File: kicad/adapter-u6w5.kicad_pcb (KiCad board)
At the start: 2 copper layers, 107.9 x 86 mm, 4 parts, among them J1 THUMB_RIGHT_SPC_KB600, J5 THUMB LEFT BAK, J6 THUMB RIGHT SPC, J8 THUMB_LEFT_BAK_KB600

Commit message: adjust board size
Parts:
- moved J1 2.54 mm to (141.6, 134.6)
- moved J5 2.54 mm to (121.4, 129.8)
- moved J6 2.54 mm to (132.1, 129.8)
- moved J8 2.54 mm to (112.4, 134.6)
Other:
- board size 107.9 x 86 mm -> 62.9 x 11.2 mm
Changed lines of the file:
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@@
     (add_net /ROW_8)
     (add_net /ROW_9)
-    (add_net GND)
     (add_net "Net-(J1-Pad1)")
     (add_net "Net-(J1-Pad10)")
@@
   )
   (module kinx:39-53-2135 (layer F.Cu)
-    (at 112.395 137.16 180)
+    (at 112.395 134.62 180)
     (descr "\"1.25 FPC CONN ASSY ZF 13\"")
     (fp_text reference J8 (at -12.827 -0.254 180) (layer F.SilkS) hide
@@
   )
   (module Connector_PinHeader_2.54mm:PinHeader_1x10_P2.54mm_Vertical (layer B.Cu)
-    (at 121.412 132.334 90)
+    (at 121.412 129.794 90)
     (descr "Through hole straight pin header, 1x10, 2.54mm pitch, single row")
     (tags "Through hole pin header THT 1x10 2.54mm single row")
@@
   )
   (module Connector_PinHeader_2.54mm:PinHeader_1x10_P2.54mm_Vertical (layer B.Cu)
-    (at 132.08 132.334 270)
+    (at 132.08 129.794 270)
     (descr "Through hole straight pin header, 1x10, 2.54mm pitch, single row")
     (tags "Through hole pin header THT 1x10 2.54mm single row")
@@
   )
   (module kinx:39-53-2135 (layer F.Cu)
-    (at 141.605 137.16 180)
+    (at 141.605 134.62 180)
     (descr "\"1.25 FPC CONN ASSY ZF 13\"")
     (fp_text reference J1 (at 11.557 -0.254 180) (layer F.SilkS) hide
@@
       (solder_mask_margin 0.0635))
   )
-  (gr_line (start 95.25 148.0036) (end 203.2 148.0036) (layer Edge.Cuts) (width 0.05))
-  (gr_line (start 203.2 148.0036) (end 203.2 62.0036) (layer Edge.Cuts) (width 0.05))
-  (gr_line (start 203.2 62.0036) (end 95.25 62.0036) (layer Edge.Cuts) (width 0.05))
-  (gr_line (start 95.25 62.0036) (end 95.25 148.0036) (layer Edge.Cuts) (width 0.05))
-  (segment (start 148.971 136.819) (end 148.931 136.779) (width 0.25) (layer F.Cu) (net 0))
+  (gr_line (start 95.25 138.176) (end 158.115 138.176) (layer Edge.Cuts) (width 0.05))
+  (gr_line (start 158.115 138.176) (end 158.115 127) (layer Edge.Cuts) (width 0.05))
+  (gr_line (start 158.115 127) (end 95.25 127) (layer Edge.Cuts) (width 0.05))
+  (gr_line (start 95.25 127) (end 95.25 138.176) (layer Edge.Cuts) (width 0.05))
+  (segment (start 148.971 134.279) (end 148.931 134.239) (width 0.25) (layer F.Cu) (net 0))
   (zone (net 9) (net_name GND) (layer F.Cu) (hatch edge 0.508)
     (priority 6)
@@
     (polygon
       (pts
-        (xy 203.1163 147.2068) (xy 95.25 147.2068) (xy 95.25 62.8004) (xy 203.1163 62.8004)
+        (xy 157.988 138.049) (xy 95.377 138.049) (xy 95.377 127.127) (xy 157.988 127.127)
       )
     )
@@
     (polygon
       (pts
-        (xy 203.1163 147.2068) (xy 95.25 147.2068) (xy 95.25 62.8004) (xy 203.1163 62.8004)
+        (xy 157.988 138.049) (xy 95.377 138.049) (xy 95.377 127.127) (xy 157.988 127.127)
       )
     )

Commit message: panelization: add mouse bites/tab and cut lines
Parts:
- added REF**: tab, panelizationtab:tab, F.Cu at (125.9, 132.7)
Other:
- board size 62.9 x 11.2 mm -> 62.9 x 11.3 mm
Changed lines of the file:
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@@
   (general
     (thickness 1.6)
-    (drawings 4)
+    (drawings 6)
     (tracks 1)
     (zones 0)
-    (modules 4)
+    (modules 5)
     (nets 12)
   )
@@
   (setup
     (last_trace_width 0.25)
+    (user_trace_width 2.54)
     (trace_clearance 0.1524)
     (zone_clearance 0.2)
@@
     (add_net "Net-(J1-Pad2)")
     (add_net "Net-(J1-Pad9)")
-    (add_net "Net-(J5-Pad10)")
-    (add_net "Net-(J5-Pad6)")
-    (add_net "Net-(J5-Pad7)")
-    (add_net "Net-(J5-Pad9)")
     (add_net "Net-(J6-Pad1)")
     (add_net "Net-(J6-Pad10)")
@@
     (add_net "Net-(J8-Pad7)")
     (add_net "Net-(J8-Pad8)")
+  )
+  (module panelizationtab:tab (layer F.Cu)
+    (at 125.857 132.715 90)
+    (fp_text reference REF** (at 0 0.5 90) (layer F.SilkS) hide
+      (effects (font (size 1 1) (thickness 0.15)))
+    )
+    (fp_text value tab (at 0 -0.5 90) (layer F.Fab) hide
+      (effects (font (size 1 1) (thickness 0.15)))
+    )
+    (pad 4 thru_hole circle (at -1.016 1.905 90) (size 0.51 0.51) (drill 0.254) (layers *.Cu *.Mask))
+    (pad 6 thru_hole circle (at 1.016 1.905 90) (size 0.51 0.51) (drill 0.254) (layers *.Cu *.Mask))
+    (pad 5 thru_hole circle (at 0 1.905 90) (size 0.51 0.51) (drill 0.254) (layers *.Cu *.Mask))
+    (pad 1 thru_hole circle (at -1.016 0 90) (size 0.51 0.51) (drill 0.254) (layers *.Cu *.Mask))
+    (pad 3 thru_hole circle (at 1.016 0 90) (size 0.51 0.51) (drill 0.254) (layers *.Cu *.Mask))
+    (pad 2 thru_hole circle (at 0 0 90) (size 0.51 0.51) (drill 0.254) (layers *.Cu *.Mask))
   )
   (module kinx:39-53-2135 (layer F.Cu)
@@
       (solder_mask_margin 0.0635))
   )
+  (gr_line (start 126.746 135.128) (end 126.746 138.303) (layer Edge.Cuts) (width 2.54))
+  (gr_line (start 126.746 127) (end 126.746 130.302) (layer Edge.Cuts) (width 2.54))
   (gr_line (start 95.25 138.176) (end 158.115 138.176) (layer Edge.Cuts) (width 0.05))
   (gr_line (start 158.115 138.176) (end 158.115 127) (layer Edge.Cuts) (width 0.05))

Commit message: route
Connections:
- net /ROW_2 renamed /ROW_2_L
- net /ROW_3 renamed /ROW_3_L
- net /ROW_4 renamed /ROW_4_L
- net /ROW_5 renamed /ROW_5_L
- net /ROW_6 renamed /ROW_6_R
- net /ROW_7 renamed /ROW_7_R
- net /ROW_8 renamed /ROW_8_R
- net /ROW_9 renamed /ROW_9_R
- J1 pad 1: (no net) -> Net-(J1-Pad1)
- J1 pad 10: (no net) -> Net-(J1-Pad10)
- J1 pad 11: (no net) -> Net-(J1-Pad11)
- J1 pad 12: (no net) -> Net-(J1-Pad12)
- J1 pad 13: (no net) -> Net-(J1-Pad13)
- J1 pad 2: (no net) -> Net-(J1-Pad2)
- J1 pad 7: /COL_6 -> /COL_6_R
- J1 pad 8: /COL_5 -> /COL_5_R
- J1 pad 9: (no net) -> Net-(J1-Pad9)
- J5 pad 10: (no net) -> Net-(J5-Pad10)
- J5 pad 4: /COL_6 -> /COL_6_L
- J5 pad 5: /COL_5 -> /COL_5_L
- J5 pad 6: (no net) -> Net-(J5-Pad6)
- J5 pad 7: (no net) -> Net-(J5-Pad7)
- J5 pad 9: (no net) -> Net-(J5-Pad9)
- J6 pad 1: (no net) -> Net-(J6-Pad1)
- J6 pad 10: (no net) -> Net-(J6-Pad10)
- J6 pad 2: (no net) -> Net-(J6-Pad2)
- J6 pad 7: /COL_6 -> /COL_6_R
- J6 pad 8: /COL_5 -> /COL_5_R
- J6 pad 9: (no net) -> Net-(J6-Pad9)
- J8 pad 1: (no net) -> Net-(J8-Pad1)
- J8 pad 10: /COL_6 -> /COL_6_L
- J8 pad 2: (no net) -> Net-(J8-Pad2)
- J8 pad 3: (no net) -> Net-(J8-Pad3)
- J8 pad 4: (no net) -> Net-(J8-Pad4)
- J8 pad 5: (no net) -> Net-(J8-Pad5)
- J8 pad 7: (no net) -> Net-(J8-Pad7)
- J8 pad 8: (no net) -> Net-(J8-Pad8)
- J8 pad 9: /COL_5 -> /COL_5_L
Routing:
- net /ROW_4_L: track 0.00 -> 23.5 mm
- net /ROW_2_L: track 0.00 -> 20.6 mm
- net /ROW_6_R: track 0.00 -> 19.6 mm
- net /COL_5_R: track 0.00 -> 18.1 mm
- net /ROW_5_L: track 0.00 -> 15.2 mm
- net /COL_6_L: track 0.00 -> 13.8 mm
- net /ROW_7_R: track 0.00 -> 11.5 mm
- net /ROW_3_L: track 0.00 -> 11.3 mm
- net /COL_6_R: track 0.00 -> 9.87 mm
- net /ROW_8_R: track 0.00 -> 7.17 mm
- net /COL_5_L: track 0.00 -> 5.39 mm
- net /ROW_9_R: track 0.00 -> 3.97 mm
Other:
- board text added: "kinx u6w5 v2020-06-30"

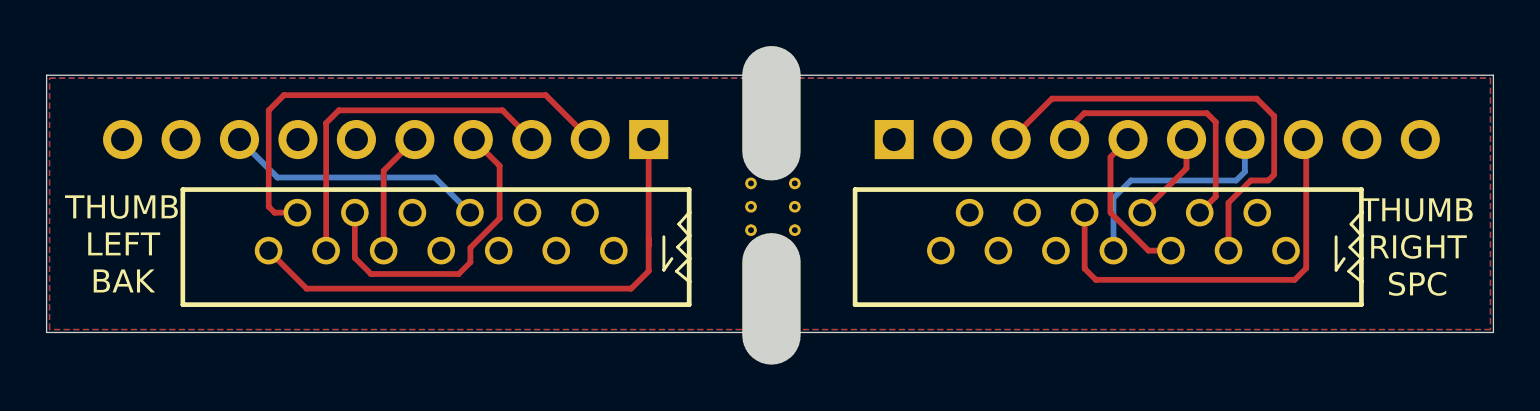
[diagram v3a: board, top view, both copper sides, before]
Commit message: cut boards apart as per oshpark support
The fab will add the required tabs.
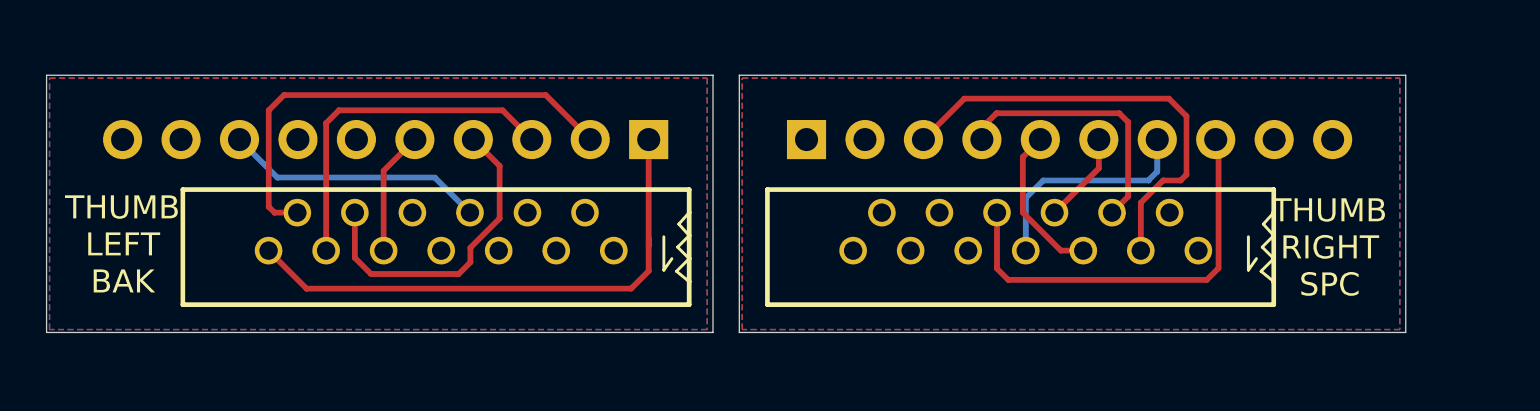
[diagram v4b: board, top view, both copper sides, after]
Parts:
- removed REF**: tab, panelizationtab:tab
- moved J1 3.81 mm to (137.8, 134.6)
- moved J6 3.81 mm to (128.3, 129.8)
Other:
- board size 62.9 x 11.3 mm -> 59.1 x 11.2 mm
- board text added: "kinx u6w5 v2020-07-02"
- board text removed: "kinx u6w5 v2020-06-30"

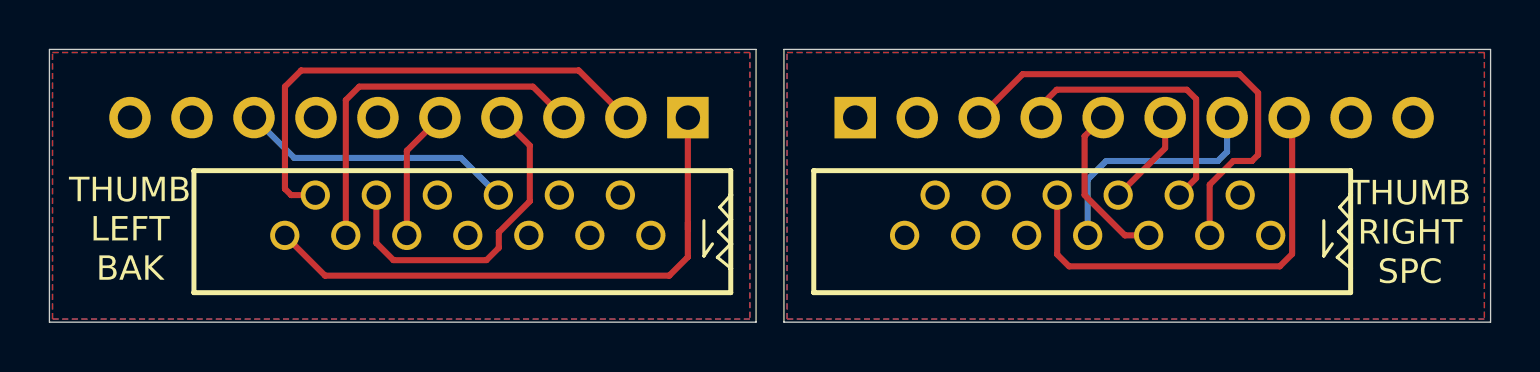
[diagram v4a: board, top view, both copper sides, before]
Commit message: move parts around, rotate correctly, re-route
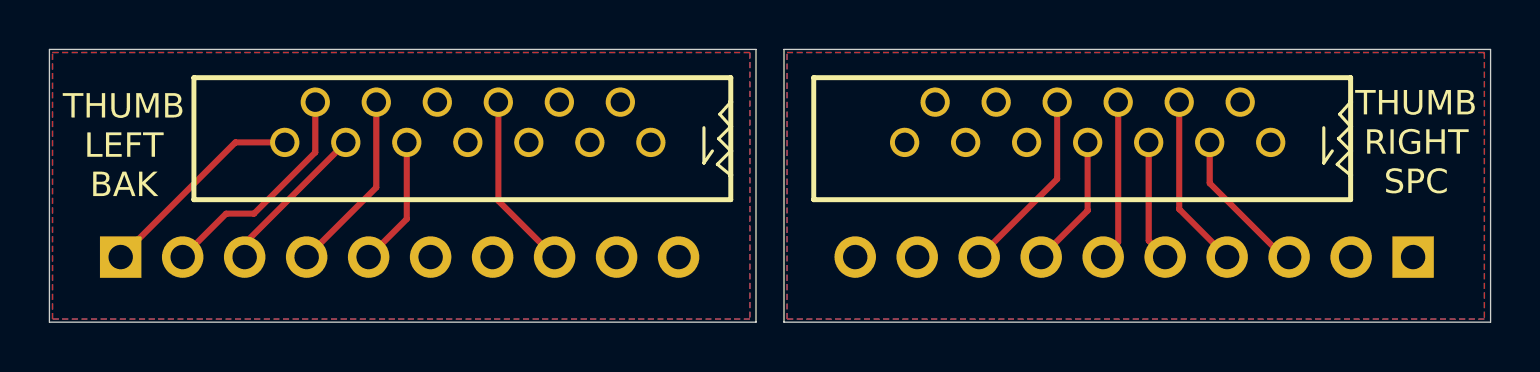
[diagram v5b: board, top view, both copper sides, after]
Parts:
- moved J5 23.9 mm to (98.2, 135.5), turned to 270 degrees
- moved J6 23.6 mm to (151.1, 135.5), turned to 90 degrees
- moved J1 3.81 mm to (137.8, 130.8)
- moved J8 3.81 mm to (112.4, 130.8)
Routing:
- net /ROW_4_L: track 23.5 -> 8.67 mm
- net /ROW_6_R: track 19.6 -> 6.18 mm
- net /ROW_2_L: track 20.6 -> 9.27 mm
- net /COL_5_R: track 18.1 -> 7.67 mm
- net /ROW_5_L: track 15.2 -> 6.42 mm
- net /COL_6_L: track 13.8 -> 7.53 mm
- net /COL_6_R: track 9.87 -> 5.49 mm
- net /ROW_7_R: track 11.5 -> 7.16 mm
- net /ROW_3_L: track 11.3 -> 7.30 mm
- net /ROW_9_R: track 3.97 -> 6.60 mm
- net /ROW_8_R: track 7.17 -> 4.98 mm
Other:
- board text added: "kinx u6w5 v2020-07-20"
- board text removed: "kinx u6w5 v2020-07-02"
